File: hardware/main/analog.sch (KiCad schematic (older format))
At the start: 44 parts, among them U2 LM324, U301 LM324

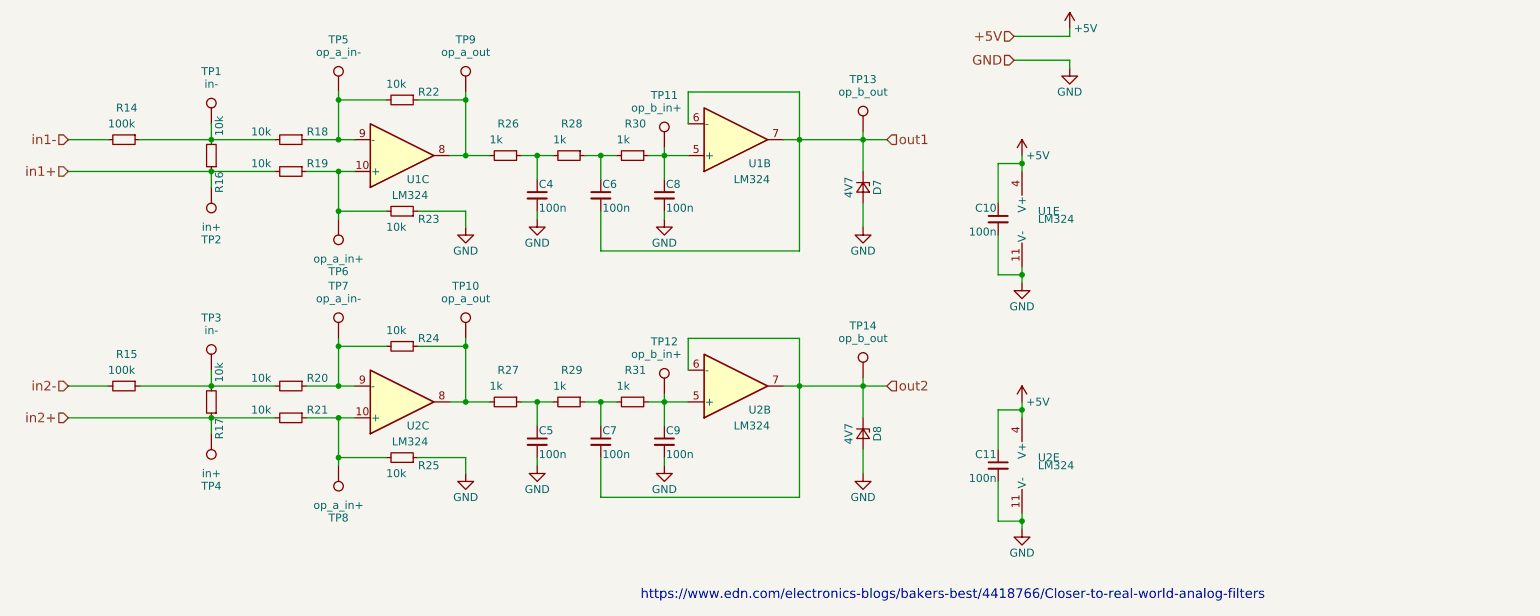
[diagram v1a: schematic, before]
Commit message: Abstração do esquemático modificada para separar as duas placas e mostrar a conexão entre elas na folha principal
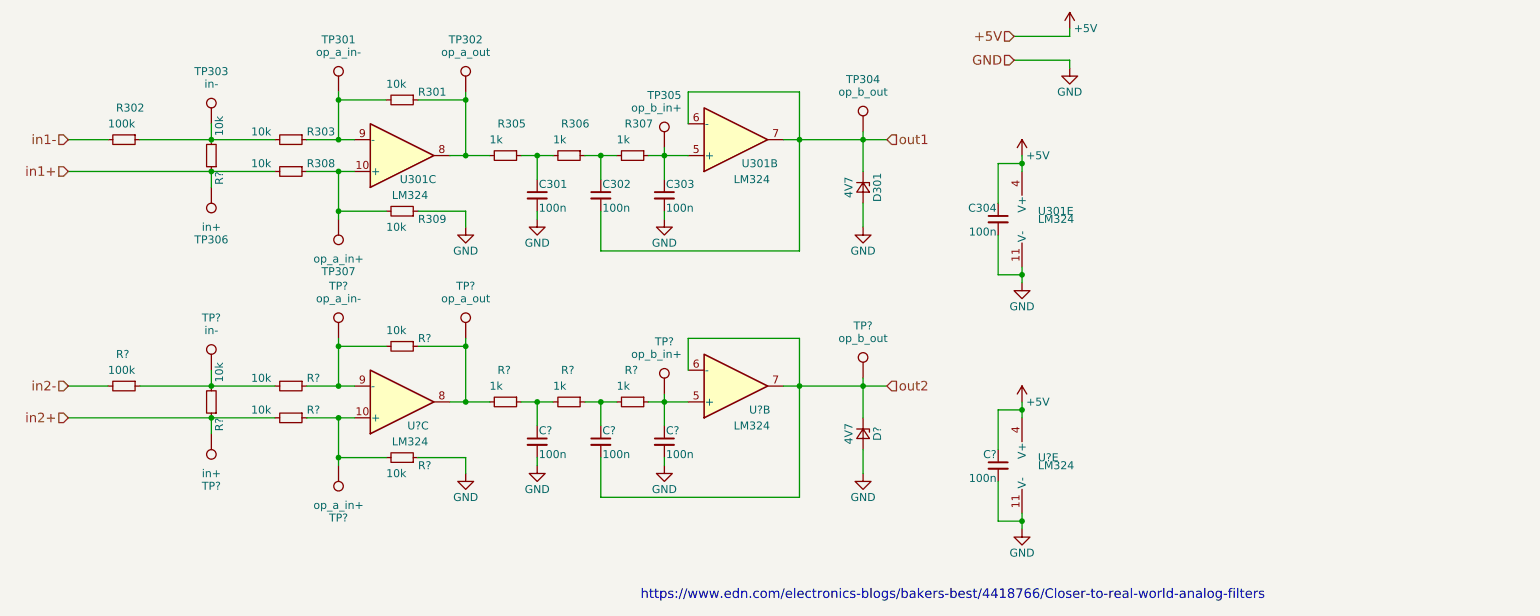
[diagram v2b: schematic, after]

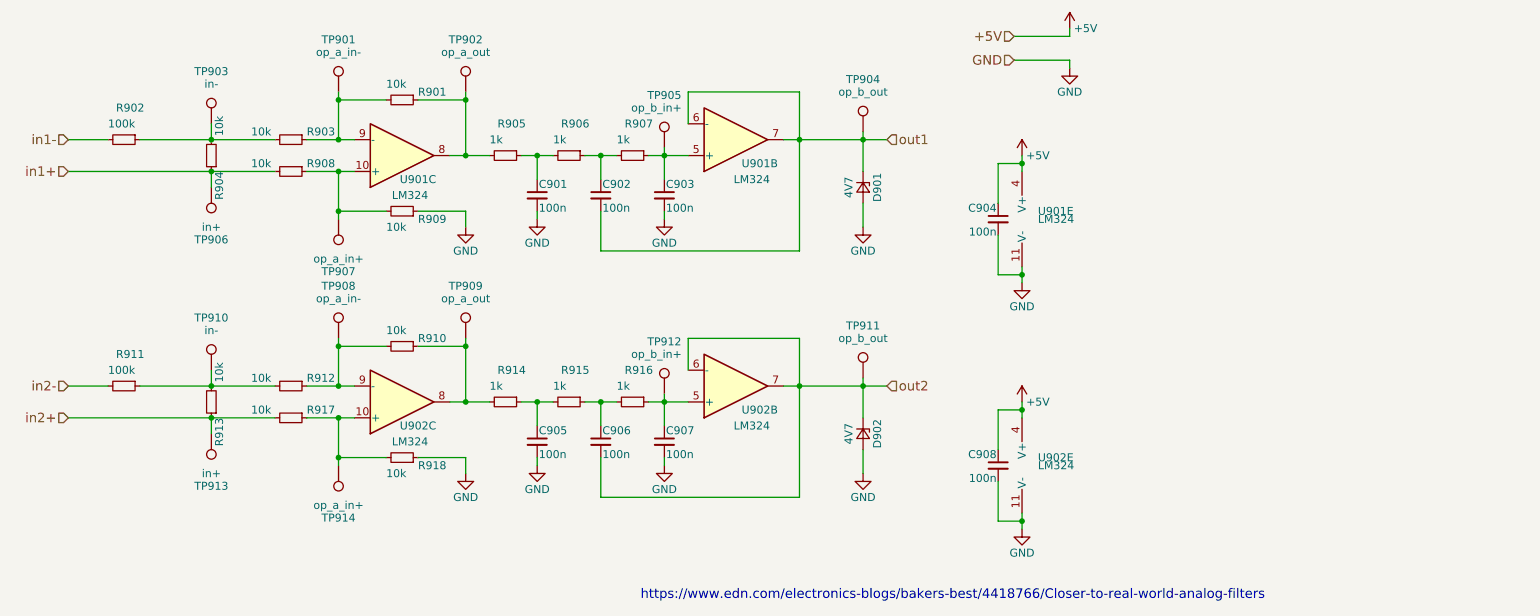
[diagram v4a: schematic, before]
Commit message: Analog passado para o Charger
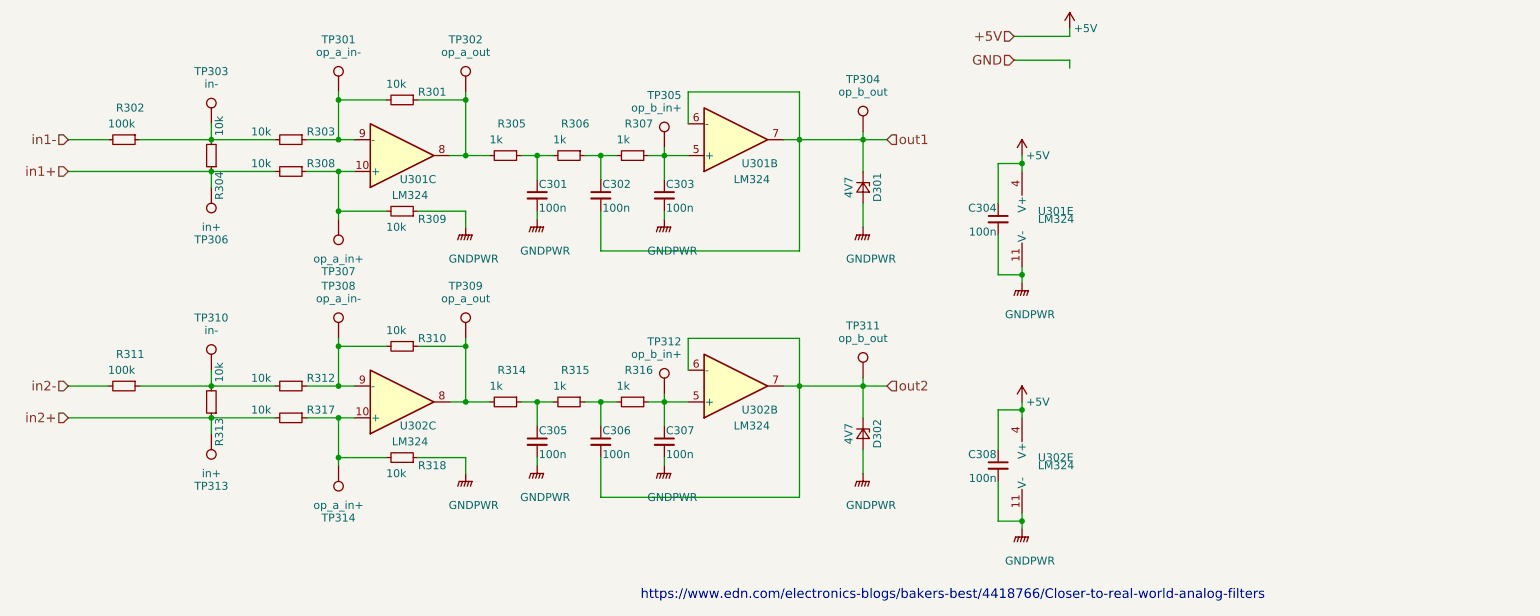
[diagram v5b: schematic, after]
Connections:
- net GND: no longer C11.2, C301.2, C303.2, C304.2, C5.2, C9.2, D301.2 (A), D8.2 (A), R25.1, R309.1, U2.11 (V-), U301.11 (V-)
- new net GNDPWR: C11.2, C301.2, C303.2, C304.2, C5.2, C9.2, D301.2 (A), D8.2 (A), R25.1, R309.1, U2.11 (V-), U301.11 (V-)

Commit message: Analog passado para o Charger
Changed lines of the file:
@@
 Wire Wire Line
 	7850 3950 7850 4100
-Text HLabel 8800 2900 0    60   Input ~ 0
-+5V
-Text HLabel 8800 3050 0    60   Input ~ 0
-GND
-$Comp
-L power:+5V #PWR0301
-U 1 1 5AAC3254
-P 9150 2850
-AR Path="/5AAC3254" Ref="#PWR0301"  Part="1"
-AR Path="/5AAC947C/5AAC3254" Ref="#PWR0301"  Part="1"
-AR Path="/5C9FC045/5AAC3254" Ref="#PWR015"  Part="1"
-AR Path="/5CA4DC1F/5CA5A61A/5AAC3254" Ref="#PWR0141"  Part="1"
-AR Path="/5C9C4D6B/5CBAEDA0/5AAC3254" Ref="#PWR0301"  Part="1"
-AR Path="/5CBD2CE3/5CBAEDA0/5AAC3254" Ref="#PWR?"  Part="1"
-F 0 "#PWR0301" H 9150 2700 50  0001 C CNN
-F 1 "+5V" H 9250 2850 50  0000 C CNN
-F 2 "" H 9150 2850 50  0001 C CNN
-F 3 "" H 9150 2850 50  0001 C CNN
-	1    9150 2850
-	1    0    0    -1
-$EndComp
-Wire Wire Line
-	9150 2900 8800 2900
-Wire Wire Line
-	8800 3050 9150 3050
 Text HLabel 2850 3550 0    60   Input ~ 0
 in1-
@@
 https://www.edn.com/electronics-blogs/bakers-best/4418766/Closer-to-real-world-analog-filters
 Wire Wire Line
-	9150 3050 9150 3100
-Wire Wire Line
-	9150 2850 9150 2900
-Wire Wire Line
 	4550 3550 4650 3550

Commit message: Esquematico primeira versão Erro de referencia dos componentes na PCB com os do Esquematico solucionados
Pontos de teste adicionados
Alimentar o analog com +12V
Adicionar Snubber para os reles
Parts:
- added TP13: +12V, TestPoint:TestPoint_Pad_2.0x2.0mm, symbol Connector:TestPoint
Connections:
- net +5V renamed +12VA
- net +12VA: now also TP13.1
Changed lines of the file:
@@
 EESchema Schematic File Version 4
 LIBS:main-cache
-EELAYER 29 0
+EELAYER 26 0
 EELAYER END
 $Descr A4 11693 8268
@@
 Wire Wire Line
 	8700 3700 8700 3950
-$Comp
-L power:+5V #PWR0303
-U 1 1 5BE86FFF
-P 8850 3650
-AR Path="/5BE86FFF" Ref="#PWR0303"  Part="1"
-AR Path="/5AAC947C/5BE86FFF" Ref="#PWR0303"  Part="1"
-AR Path="/5C9FC045/5BE86FFF" Ref="#PWR011"  Part="1"
-AR Path="/5CA4DC1F/5CA5A61A/5BE86FFF" Ref="#PWR0143"  Part="1"
-AR Path="/5C9C4D6B/5CBAEDA0/5BE86FFF" Ref="#PWR0303"  Part="1"
-AR Path="/5CBD2CE3/5CBAEDA0/5BE86FFF" Ref="#PWR?"  Part="1"
-F 0 "#PWR0303" H 8850 3500 50  0001 C CNN
-F 1 "+5V" H 8950 3650 50  0000 C CNN
-F 2 "" H 8850 3650 50  0001 C CNN
-F 3 "" H 8850 3650 50  0001 C CNN
-	1    8850 3650
-	1    0    0    -1
-$EndComp
 Wire Wire Line
 	8850 3650 8850 3700
@@
 Wire Wire Line
 	8700 5250 8700 5500
-$Comp
-L power:+5V #PWR?
-U 1 1 5CA047B6
-P 8850 5200
-AR Path="/5CA047B6" Ref="#PWR?"  Part="1"
-AR Path="/5AAC947C/5CA047B6" Ref="#PWR?"  Part="1"
-AR Path="/5C9FC045/5CA047B6" Ref="#PWR013"  Part="1"
-AR Path="/5CA4DC1F/5CA5A61A/5CA047B6" Ref="#PWR0149"  Part="1"
-AR Path="/5C9C4D6B/5CBAEDA0/5CA047B6" Ref="#PWR0309"  Part="1"
-AR Path="/5CBD2CE3/5CBAEDA0/5CA047B6" Ref="#PWR?"  Part="1"
-F 0 "#PWR0309" H 8850 5050 50  0001 C CNN
-F 1 "+5V" H 8950 5200 50  0000 C CNN
-F 2 "" H 8850 5200 50  0001 C CNN
-F 3 "" H 8850 5200 50  0001 C CNN
-	1    8850 5200
-	1    0    0    -1
-$EndComp
 Wire Wire Line
 	8850 5200 8850 5250
@@
 	1    0    0    -1
 $EndComp
+$Comp
+L power:+12VA #PWR0147
+U 1 1 5CA79643
+P 8850 3650
+F 0 "#PWR0147" H 8850 3500 50  0001 C CNN
+F 1 "+12VA" H 8865 3823 50  0000 C CNN
+F 2 "" H 8850 3650 50  0001 C CNN
+F 3 "" H 8850 3650 50  0001 C CNN
+	1    8850 3650
+	1    0    0    -1
+$EndComp
+$Comp
+L power:+12VA #PWR0148
+U 1 1 5CA79715
+P 8850 5200
+F 0 "#PWR0148" H 8850 5050 50  0001 C CNN
+F 1 "+12VA" H 8865 5373 50  0000 C CNN
+F 2 "" H 8850 5200 50  0001 C CNN
+F 3 "" H 8850 5200 50  0001 C CNN
+	1    8850 5200
+	1    0    0    -1
+$EndComp
+Text HLabel 9100 3550 2    50   Output ~ 0
++12V
+Wire Wire Line
+	9100 3550 9100 3700
+$Comp
+L Connector:TestPoint TP?
+U 1 1 5CB26FD3
+P 9550 3700
+AR Path="/5CB26FD3" Ref="TP?"  Part="1"
+AR Path="/5AAC947C/5CB26FD3" Ref="TP?"  Part="1"
+AR Path="/5C9FC045/5CB26FD3" Ref="TP?"  Part="1"
+AR Path="/5CA4DC1F/5CA5A61A/5CB26FD3" Ref="TP?"  Part="1"
+AR Path="/5C9C4D6B/5CBAEDA0/5CB26FD3" Ref="TP13"  Part="1"
+AR Path="/5CBD2CE3/5CBAEDA0/5CB26FD3" Ref="TP?"  Part="1"
+F 0 "TP13" H 9550 4000 50  0000 C BNN
+F 1 "+12V" H 9550 3950 50  0000 C CNN
+F 2 "TestPoint:TestPoint_Pad_2.0x2.0mm" H 9550 3700 50  0001 C CNN
+F 3 "" H 9550 3700 50  0001 C CNN
+	1    9550 3700
+	1    0    0    -1
+$EndComp
+Wire Wire Line
+	8850 3700 9100 3700
+Wire Wire Line
+	9100 3700 9550 3700
+Connection ~ 9100 3700
 $EndSCHEMATC

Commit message: Footprints
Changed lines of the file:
@@
 	9100 3700 9550 3700
 Connection ~ 9100 3700
+Text HLabel 9000 5950 2    50   Output ~ 0
+GND
+Wire Wire Line
+	8850 5950 9000 5950
 $EndSCHEMATC
